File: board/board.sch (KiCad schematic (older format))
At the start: 52 parts, among them J1 programmer, J2 USB_B_Micro, Q1 Q_PMOS_DSG, Q2 Q_NMOS_GSD, U1 ESP-WROOM-02, U2 RT8097AHGB, U3 RT8097AHGB, U4 NPIC6C596, U5 NPIC6C596

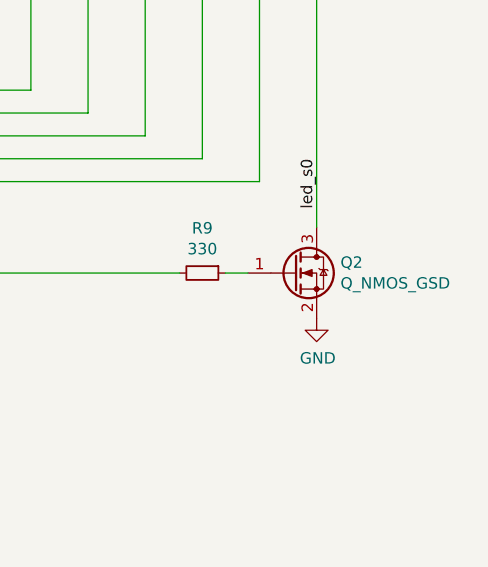
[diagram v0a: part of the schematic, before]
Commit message: Update transistor partno
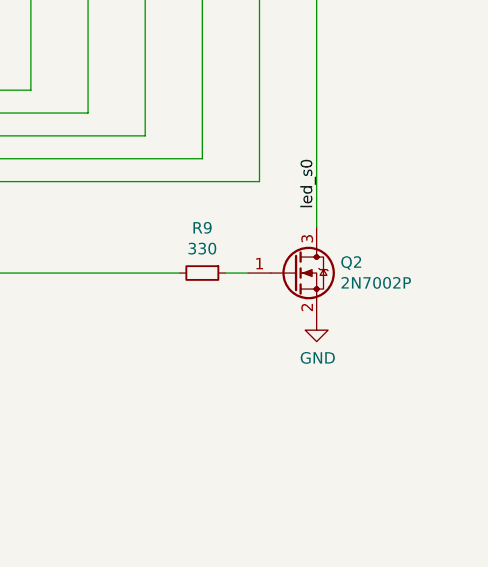
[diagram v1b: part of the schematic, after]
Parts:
- Q2: value Q_NMOS_GSD -> 2N7002P
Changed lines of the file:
@@
 P 10700 4300
 F 0 "Q2" H 10904 4346 50  0000 L CNN
-F 1 "Q_NMOS_GSD" H 10904 4255 50  0000 L CNN
+F 1 "2N7002P" H 10904 4255 50  0000 L CNN
 F 2 "Package_TO_SOT_SMD:SOT-23" H 10900 4400 50  0001 C CNN
 F 3 "~" H 10700 4300 50  0001 C CNN

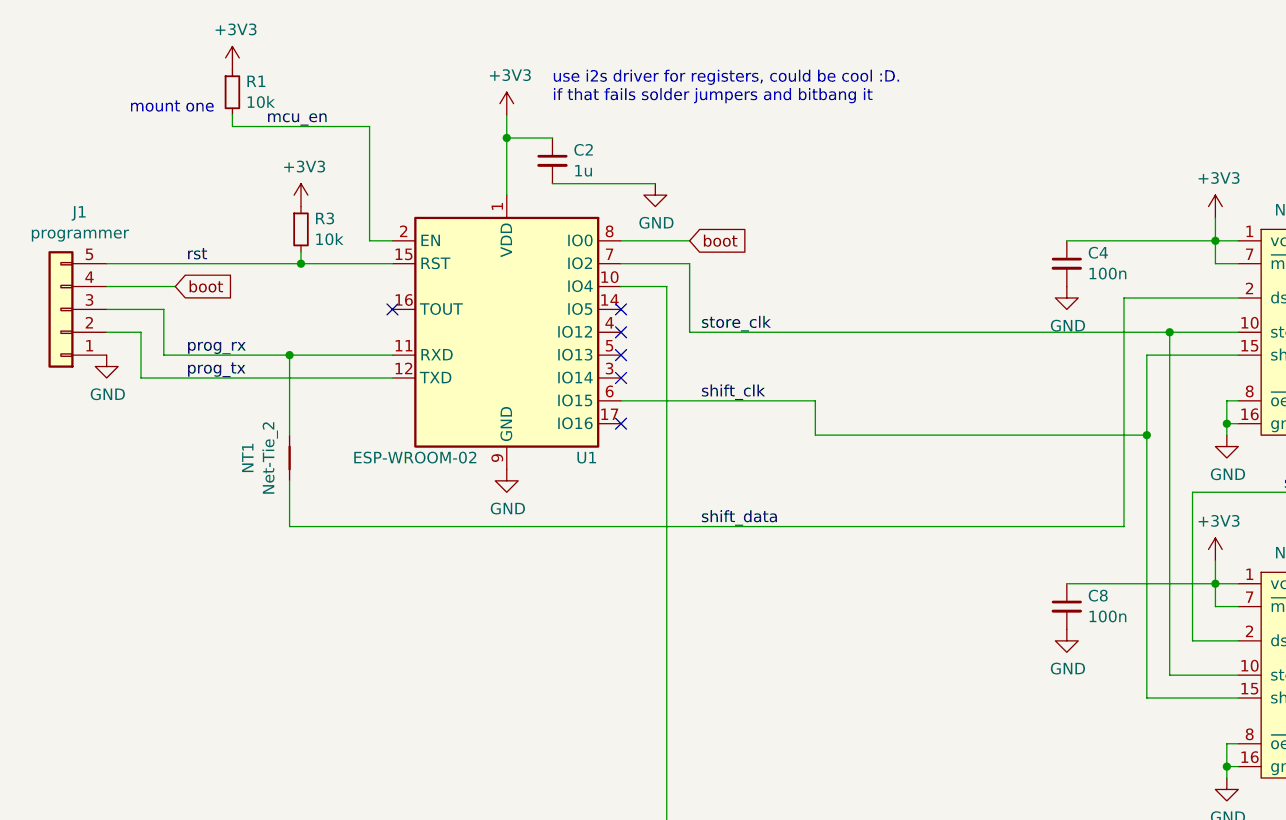
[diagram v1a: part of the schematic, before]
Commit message: Add missing passives from bringup
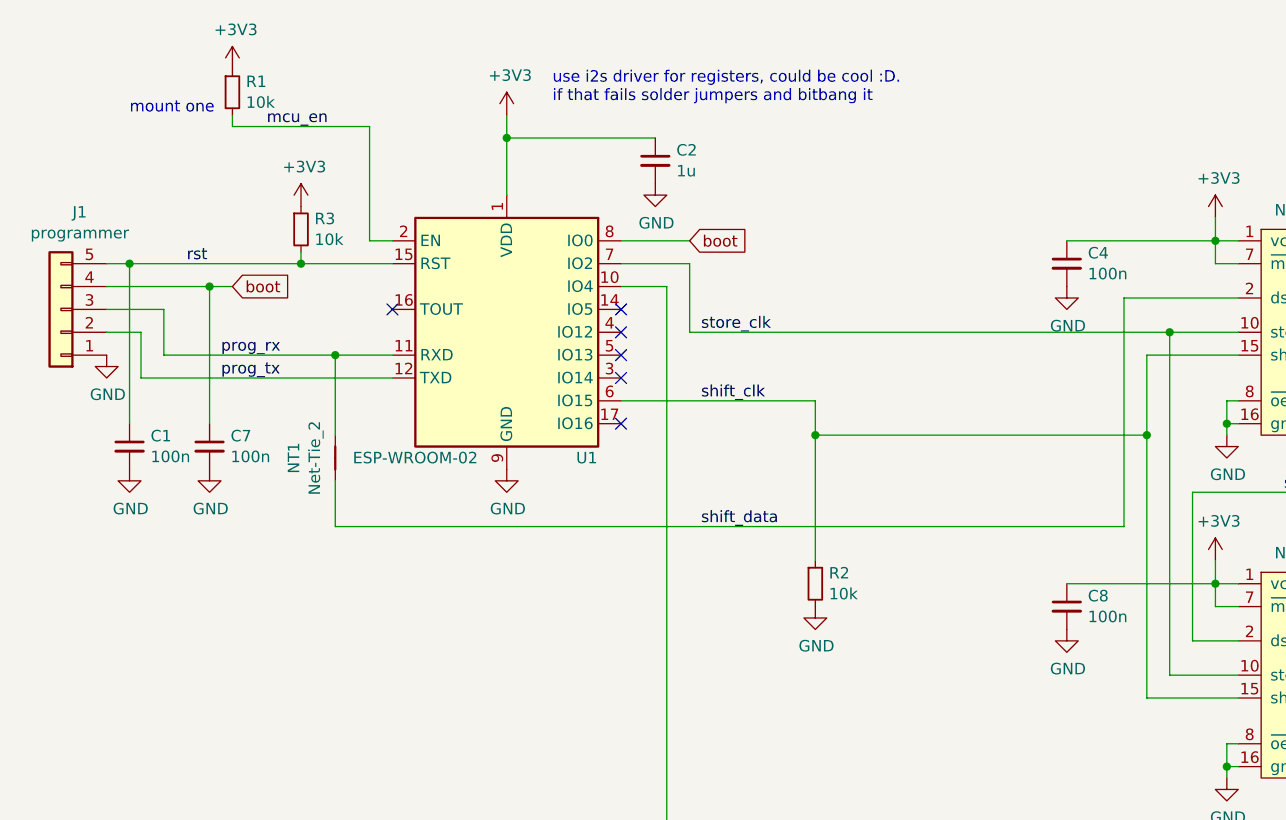
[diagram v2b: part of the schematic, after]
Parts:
- added C1, C7: 100n, Capacitor_SMD:C_0603_1608Metric, symbol Device:C_Small
- added R2: 10k, Resistor_SMD:R_0603_1608Metric, symbol Device:R_Small
- FB1: footprint Inductor_SMD:L_0805_2012Metric -> Inductor_SMD:L_0603_1608Metric_Pad1.05x0.95mm_HandSolder
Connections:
- net GND: now also C1.2, C7.2, R2.2
- net boot: now also C7.1
- net rst: now also C1.1
- net shift_clk: now also R2.1
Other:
- moved on the sheet: C2, NT1
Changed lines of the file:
@@
 F 0 "FB1" V 2963 5550 50  0000 C CNN
 F 1 "1A" V 3054 5550 50  0000 C CNN
-F 2 "Inductor_SMD:L_0805_2012Metric" V 3130 5550 50  0001 C CNN
+F 2 "Inductor_SMD:L_0603_1608Metric_Pad1.05x0.95mm_HandSolder" V 3130 5550 50  0001 C CNN
 F 3 "~" H 3200 5550 50  0001 C CNN
 	1    3200 5550
@@
 Connection ~ 1700 1800
 Wire Wire Line
-	850  1800 1700 1800
-Wire Wire Line
 	1000 2300 2100 2300
-Connection ~ 1650 2200
-Wire Wire Line
-	1100 2200 1650 2200
 Text Label 3450 2950 0    50   ~ 0
 shift_data
 Wire Wire Line
-	1650 2750 1650 2950
-Wire Wire Line
-	1650 2200 2100 2200
-Wire Wire Line
-	1650 2550 1650 2200
+	1850 2750 1850 2950
+Wire Wire Line
+	1850 2550 1850 2200
 $Comp
 L Device:Net-Tie_2 NT1
 U 1 1 61328909
-P 1650 2650
-F 0 "NT1" H 1650 2831 50  0000 C CNN
-F 1 "Net-Tie_2" H 1650 2740 50  0000 C CNN
-F 2 "NetTie:NetTie-2_SMD_Pad0.5mm" H 1650 2650 50  0001 C CNN
-F 3 "~" H 1650 2650 50  0001 C CNN
-	1    1650 2650
+P 1850 2650
+F 0 "NT1" H 1850 2831 50  0000 C CNN
+F 1 "Net-Tie_2" H 1850 2740 50  0000 C CNN
+F 2 "NetTie:NetTie-2_SMD_Pad0.5mm" H 1850 2650 50  0001 C CNN
+F 3 "~" H 1850 2650 50  0001 C CNN
+	1    1850 2650
 	0    -1   -1   0
 $EndComp
@@
 Text Label 1200 1800 0    50   ~ 0
 rst
-Text Label 1200 2300 0    50   ~ 0
+Text Label 1350 2300 0    50   ~ 0
 prog_tx
-Text Label 1200 2200 0    50   ~ 0
+Text Label 1350 2200 0    50   ~ 0
 prog_rx
 Text GLabel 3400 1700 2    50   Input ~ 0
 boot
-Text GLabel 1150 1900 2    50   Input ~ 0
+Text GLabel 1400 1900 2    50   Input ~ 0
 boot
 Wire Wire Line
-	850  1900 1150 1900
-Wire Wire Line
 	1100 2000 850  2000
-Wire Wire Line
-	1100 2200 1100 2000
 Wire Wire Line
 	1000 2100 850  2100
@@
 	1    0    0    -1
 $EndComp
-Wire Wire Line
-	2800 1450 3250 1450
-Wire Wire Line
-	2600 1250 2800 1250
 $Comp
 L Device:C_Small C4
@@
 L Device:C_Small C2
 U 1 1 6121A66F
-P 2800 1350
-F 0 "C2" H 2892 1396 50  0000 L CNN
-F 1 "1u" H 2892 1305 50  0000 L CNN
-F 2 "Capacitor_SMD:C_0603_1608Metric" H 2800 1350 50  0001 C CNN
-F 3 "~" H 2800 1350 50  0001 C CNN
-	1    2800 1350
+P 3250 1350
+F 0 "C2" H 3342 1396 50  0000 L CNN
+F 1 "1u" H 3342 1305 50  0000 L CNN
+F 2 "Capacitor_SMD:C_0603_1608Metric" H 3250 1350 50  0001 C CNN
+F 3 "~" H 3250 1350 50  0001 C CNN
+	1    3250 1350
 	1    0    0    -1
 $EndComp
@@
 NoConn ~ 3100 2500
 Wire Wire Line
-	1650 2950 5300 2950
-Wire Wire Line
 	3950 2550 5400 2550
 Wire Wire Line
@@
 	1    0    0    -1
 $EndComp
+$Comp
+L Device:C_Small C1
+U 1 1 6199D2C8
+P 950 2600
+F 0 "C1" H 1042 2646 50  0000 L CNN
+F 1 "100n" H 1042 2555 50  0000 L CNN
+F 2 "Capacitor_SMD:C_0603_1608Metric" H 950 2600 50  0001 C CNN
+F 3 "~" H 950 2600 50  0001 C CNN
+	1    950  2600
+	1    0    0    -1
+$EndComp
+$Comp
+L power:GND #PWR0102
+U 1 1 6199DA35
+P 950 2700
+F 0 "#PWR0102" H 950 2450 50  0001 C CNN
+F 1 "GND" H 955 2527 50  0000 C CNN
+F 2 "" H 950 2700 50  0001 C CNN
+F 3 "" H 950 2700 50  0001 C CNN
+	1    950  2700
+	1    0    0    -1
+$EndComp
+$Comp
+L Device:R_Small R2
+U 1 1 6199E4A9
+P 3950 3200
+F 0 "R2" H 4009 3246 50  0000 L CNN
+F 1 "10k" H 4009 3155 50  0000 L CNN
+F 2 "Resistor_SMD:R_0603_1608Metric" H 3950 3200 50  0001 C CNN
+F 3 "~" H 3950 3200 50  0001 C CNN
+	1    3950 3200
+	1    0    0    -1
+$EndComp
+Wire Wire Line
+	3950 3100 3950 2550
+Wire Wire Line
+	850  1800 950  1800
+Connection ~ 3950 2550
+$Comp
+L power:GND #PWR0103
+U 1 1 619A705E
+P 3950 3300
+F 0 "#PWR0103" H 3950 3050 50  0001 C CNN
+F 1 "GND" H 3955 3127 50  0000 C CNN
+F 2 "" H 3950 3300 50  0001 C CNN
+F 3 "" H 3950 3300 50  0001 C CNN
+	1    3950 3300
+	1    0    0    -1
+$EndComp
+Wire Wire Line
+	1100 2200 1100 2000
+Wire Wire Line
+	950  2500 950  1800
+Connection ~ 950  1800
+Wire Wire Line
+	950  1800 1700 1800
+Wire Wire Line
+	2600 1250 3250 1250
+Connection ~ 1850 2200
+Wire Wire Line
+	1850 2200 2100 2200
+Wire Wire Line
+	1850 2950 5300 2950
+Wire Wire Line
+	1100 2200 1850 2200
+$Comp
+L Device:C_Small C7
+U 1 1 619DD11C
+P 1300 2600
+F 0 "C7" H 1392 2646 50  0000 L CNN
+F 1 "100n" H 1392 2555 50  0000 L CNN
+F 2 "Capacitor_SMD:C_0603_1608Metric" H 1300 2600 50  0001 C CNN
+F 3 "~" H 1300 2600 50  0001 C CNN
+	1    1300 2600
+	1    0    0    -1
+$EndComp
+$Comp
+L power:GND #PWR0104
+U 1 1 619DD122
+P 1300 2700
+F 0 "#PWR0104" H 1300 2450 50  0001 C CNN
+F 1 "GND" H 1305 2527 50  0000 C CNN
+F 2 "" H 1300 2700 50  0001 C CNN
+F 3 "" H 1300 2700 50  0001 C CNN
+	1    1300 2700
+	1    0    0    -1
+$EndComp
+Wire Wire Line
+	850  1900 1300 1900
+Wire Wire Line
+	1300 1900 1300 2500
+Connection ~ 1300 1900
+Wire Wire Line
+	1300 1900 1400 1900
 $EndSCHEMATC
